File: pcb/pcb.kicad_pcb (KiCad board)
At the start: 2 copper layers, 57.1 x 57.2 mm, 20 parts

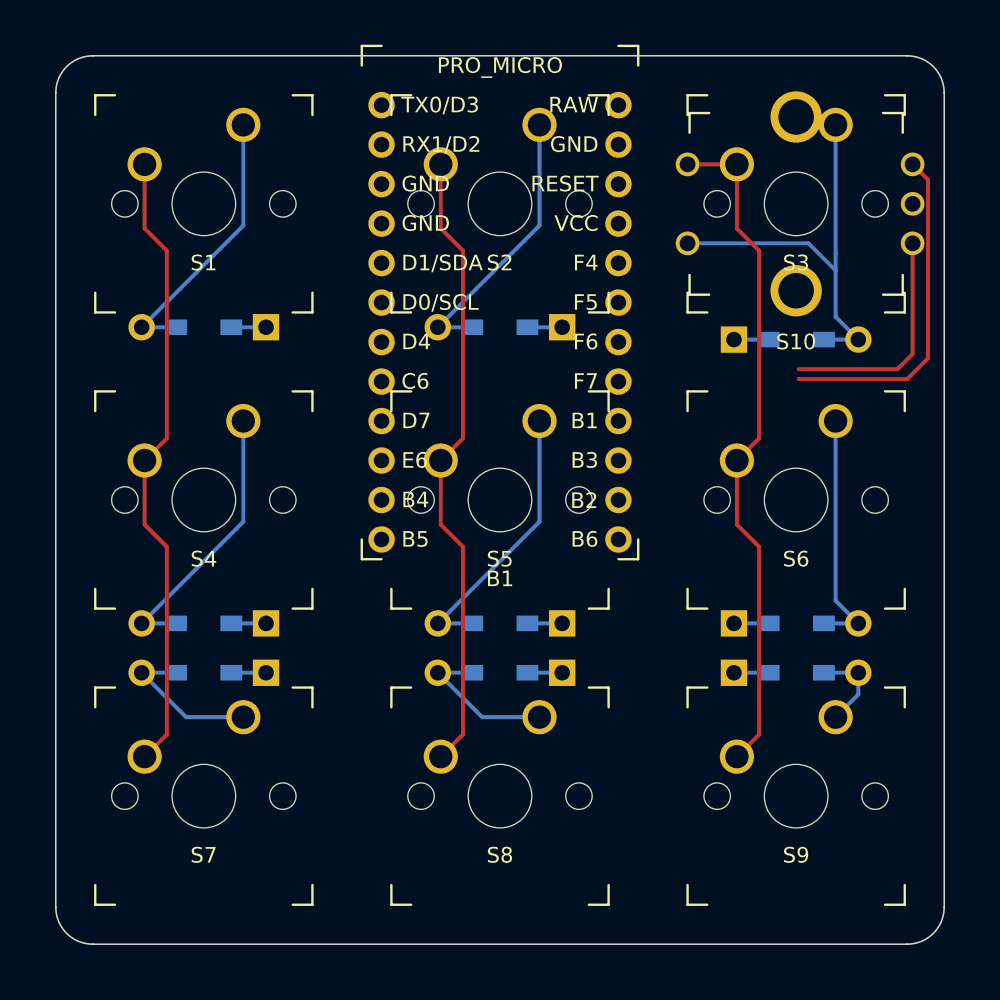
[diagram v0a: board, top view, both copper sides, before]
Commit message: 🚧 Multiple changes - Re-add reset in the form of a jumper - Add mounting holes - Rotate encoder to have enough space for the mounting holes
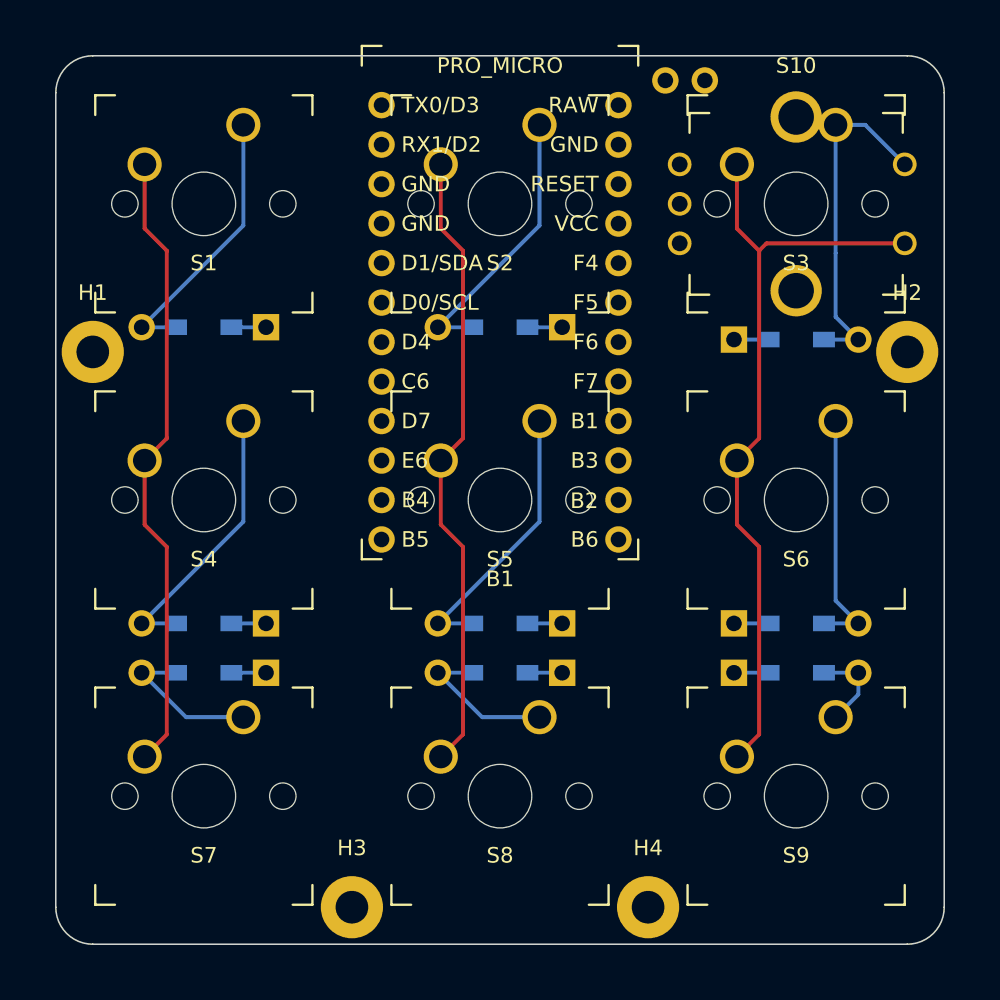
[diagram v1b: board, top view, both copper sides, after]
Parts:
- added H1: MOUNTING_HOLE, ElsassKabel:MOUNTING_HOLE_M2_PAD, F.Cu at (122.2, 86.5)
- added H2: MOUNTING_HOLE, ElsassKabel:MOUNTING_HOLE_M2_PAD, F.Cu at (174.6, 86.5)
- added H3: MOUNTING_HOLE, ElsassKabel:MOUNTING_HOLE_M2_PAD, F.Cu at (138.9, 122.2)
- added H4: MOUNTING_HOLE, ElsassKabel:MOUNTING_HOLE_M2_PAD, F.Cu at (158.0, 122.2)
- added Reset: CONN_2PIN, ElsassKabel:CONN_2PIN, B.Cu at (160.3, 69.1)
- turned S10 to 0 degrees
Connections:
- B1 pad 22: unconnected-(B1-Pad22) -> reset
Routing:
- net encB: track 21.8 -> 0.00 mm
- net encA: track 14.9 -> 0.00 mm
- net col2: track 43.6 -> 50.0 mm
- net rotB: track 26.9 -> 22.1 mm

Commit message: 🚧 Finish wiring
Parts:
- removed Reset: CONN_2PIN, ElsassKabel:CONN_2PIN
- added P1: CONN_2PIN, ElsassKabel:CONN_2PIN, F.Cu at (138.9, 69.1)
- B1: moved to B.Cu
- moved B1 4.29 mm to (148.4, 87.6), turned to 180 degrees
- turned D2 to 180 degrees
- turned D5 to 180 degrees
- turned D8 to 180 degrees
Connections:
- B1 pad 10: col0 -> col2
- B1 pad 12: col2 -> col0
- B1 pad 16: encB -> unconnected-(B1-Pad16)
- B1 pad 17: encA -> unconnected-(B1-Pad17)
- B1 pad 8: unconnected-(B1-Pad8) -> encA
- B1 pad 9: unconnected-(B1-Pad9) -> encB
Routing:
- net col0: track 40.5 -> 87.2 mm
- net row0: track 6.70 -> 51.0 mm
- net row2: track 6.70 -> 44.1 mm
- net row1: track 6.70 -> 40.7 mm
- net encA: track 0.00 -> 19.9 mm
- net encB: track 0.00 -> 17.3 mm
- net reset: track 0.00 -> 12.3 mm
- net col1: track 40.5 -> 51.0 mm
- net col2: track 50.0 -> 57.7 mm
- net Net-(D8-Pad1): track 9.94 -> 5.68 mm
- net Net-(D5-Pad1): track 17.9 -> 15.8 mm
- net Net-(D2-Pad1): track 17.9 -> 15.8 mm
- added copper zone on B.Cu, net GND
- added copper zone on F.Cu, net GND
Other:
- board text added: "Reset"
